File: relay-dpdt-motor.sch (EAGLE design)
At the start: 4 parts, among them K1 4052

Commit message: eagle prewired
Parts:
- added D1: 1N4004, adafruit:1N4004
- added J1, J2: 1X2-3.5MM, adafruit:1X2-3.5MM
- added JP1: (no value), adafruit:PINHD-1X3CB
- added R2: (no value), adafruit:R-US_0204/7
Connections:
- new net +12V: D1.C, J1.2, K11.1, K12.P
- new net GND: J1.1, JP1.1, Q1.E, Q2.S
- new net N$1: Q1.B, R1.2
- new net N$2: K11.2, Q1.C
- new net N$3: Q2.G, R2.2
- new net N$5: D1.A, K13.P, Q2.D
- new net N$6: J2.1, K12.S, K13.O
- new net N$7: J2.2, K12.O, K13.S
- new net N$8: JP1.2, R2.1
- new net N$9: JP1.3, R1.1
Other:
- moved on the sheet: K1, Q1, Q2, R1
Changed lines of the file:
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@@
 <setting verticaltext="up"/>
 </settings>
-<grid distance="0.1" unitdist="inch" unit="inch" style="lines" multiple="1" display="no" altdistance="0.01" altunitdist="inch" altunit="inch"/>
+<grid distance="50" unitdist="mil" unit="mil" style="lines" multiple="1" display="no" altdistance="25" altunitdist="mil" altunit="mil"/>
 <layers>
 <layer number="1" name="Top" color="4" fill="1" visible="no" active="no"/>
@@
 <part name="R1" library="adafruit" deviceset="R-US_" device="0204/7"/>
 <part name="Q2" library="adafruit" deviceset="MOSFET-N" device="GDS_TO220V"/>
+<part name="D1" library="adafruit" deviceset="1N4004" device=""/>
+<part name="J1" library="adafruit" deviceset="1X2" device="-3.5MM"/>
+<part name="+12V1" library="dp_devices" deviceset="SUPPLY_+12V" device=""/>
+<part name="R2" library="adafruit" deviceset="R-US_" device="0204/7"/>
+<part name="U$2" library="microbuilder" deviceset="GND" device=""/>
+<part name="J2" library="adafruit" deviceset="1X2" device="-3.5MM"/>
+<part name="JP1" library="adafruit" deviceset="PINHD-1X3" device="CB"/>
+<part name="U$3" library="microbuilder" deviceset="GND" device=""/>
+<part name="U$1" library="microbuilder" deviceset="GND" device=""/>
 </parts>
 <sheets>
@@
 </plain>
 <instances>
-<instance part="K1" gate="1" x="34.29" y="76.2"/>
-<instance part="K1" gate="2" x="52.07" y="76.2"/>
-<instance part="K1" gate="3" x="52.07" y="60.96"/>
-<instance part="Q1" gate="Q" x="30.48" y="57.15"/>
-<instance part="R1" gate="G$1" x="22.86" y="44.45"/>
-<instance part="Q2" gate="G$1" x="33.02" y="38.1"/>
+<instance part="K1" gate="1" x="25.4" y="74.93" smashed="yes">
+<attribute name="VALUE" x="29.21" y="70.231" size="1.778" layer="96"/>
+<attribute name="PART" x="19.05" y="77.47" size="1.778" layer="95"/>
+</instance>
+<instance part="K1" gate="2" x="50.8" y="80.01" smashed="yes" rot="R270">
+<attribute name="PART" x="50.8" y="77.47" size="1.778" layer="95" rot="R270"/>
+</instance>
+<instance part="K1" gate="3" x="50.8" y="63.5" smashed="yes" rot="R270">
+<attribute name="PART" x="50.8" y="60.96" size="1.778" layer="95" rot="R270"/>
+</instance>
+<instance part="Q1" gate="Q" x="22.86" y="63.5"/>
+<instance part="R1" gate="G$1" x="13.97" y="63.5"/>
+<instance part="Q2" gate="G$1" x="43.18" y="54.61"/>
+<instance part="D1" gate="1" x="45.72" y="71.12" smashed="yes" rot="R90">
+<attribute name="NAME" x="43.18" y="73.1774" size="1.778" layer="95" rot="R180"/>
+</instance>
+<instance part="J1" gate="G$1" x="1.27" y="80.01" rot="R180"/>
+<instance part="+12V1" gate="SUPPLY" x="25.4" y="82.55"/>
+<instance part="R2" gate="G$1" x="34.29" y="52.07"/>
+<instance part="U$2" gate="G$1" x="45.72" y="45.72"/>
+<instance part="J2" gate="G$1" x="76.2" y="71.12"/>
+<instance part="JP1" gate="A" x="6.35" y="52.07" rot="R180"/>
+<instance part="U$3" gate="G$1" x="25.4" y="46.99"/>
+<instance part="U$1" gate="G$1" x="6.35" y="73.66"/>
 </instances>
 <busses>
 </busses>
 <nets>
+<net name="N$1" class="0">
+<segment>
+<pinref part="Q1" gate="Q" pin="B"/>
+<pinref part="R1" gate="G$1" pin="2"/>
+<wire x1="19.05" y1="63.5" x2="20.32" y2="63.5" width="0.1524" layer="91"/>
+</segment>
+</net>
+<net name="+12V" class="0">
+<segment>
+<pinref part="K1" gate="2" pin="P"/>
+<pinref part="D1" gate="1" pin="C"/>
+<wire x1="45.72" y1="80.01" x2="48.26" y2="80.01" width="0.1524" layer="91"/>
+<wire x1="45.72" y1="80.01" x2="45.72" y2="73.66" width="0.1524" layer="91"/>
+<junction x="45.72" y="80.01"/>
+<pinref part="+12V1" gate="SUPPLY" pin="+12V"/>
+<pinref part="K1" gate="1" pin="1"/>
+<wire x1="25.4" y1="82.55" x2="25.4" y2="80.01" width="0.1524" layer="91"/>
+<wire x1="45.72" y1="80.01" x2="25.4" y2="80.01" width="0.1524" layer="91"/>
+<junction x="25.4" y="80.01"/>
+<pinref part="J1" gate="G$1" pin="2"/>
+<wire x1="25.4" y1="80.01" x2="6.35" y2="80.01" width="0.1524" layer="91"/>
+</segment>
+</net>
+<net name="N$2" class="0">
+<segment>
+<pinref part="K1" gate="1" pin="2"/>
+<pinref part="Q1" gate="Q" pin="C"/>
+<wire x1="25.4" y1="69.85" x2="25.4" y2="68.58" width="0.1524" layer="91"/>
+</segment>
+</net>
+<net name="GND" class="0">
+<segment>
+<pinref part="Q2" gate="G$1" pin="S"/>
+<pinref part="U$2" gate="G$1" pin="GND"/>
+<wire x1="45.72" y1="49.53" x2="45.72" y2="48.26" width="0.1524" layer="91"/>
+</segment>
+<segment>
+<pinref part="U$3" gate="G$1" pin="GND"/>
+<pinref part="JP1" gate="A" pin="1"/>
+<wire x1="25.4" y1="49.53" x2="8.89" y2="49.53" width="0.1524" layer="91"/>
+<pinref part="Q1" gate="Q" pin="E"/>
+<wire x1="25.4" y1="58.42" x2="25.4" y2="49.53" width="0.1524" layer="91"/>
+<junction x="25.4" y="49.53"/>
+</segment>
+<segment>
+<pinref part="J1" gate="G$1" pin="1"/>
+<pinref part="U$1" gate="G$1" pin="GND"/>
+<wire x1="6.35" y1="77.47" x2="6.35" y2="76.2" width="0.1524" layer="91"/>
+</segment>
+</net>
+<net name="N$3" class="0">
+<segment>
+<pinref part="Q2" gate="G$1" pin="G"/>
+<pinref part="R2" gate="G$1" pin="2"/>
+<wire x1="39.37" y1="52.07" x2="40.64" y2="52.07" width="0.1524" layer="91"/>
+</segment>
+</net>
+<net name="N$5" class="0">
+<segment>
+<pinref part="K1" gate="3" pin="P"/>
+<wire x1="48.26" y1="63.5" x2="45.72" y2="63.5" width="0.1524" layer="91"/>
+<pinref part="Q2" gate="G$1" pin="D"/>
+<wire x1="45.72" y1="63.5" x2="45.72" y2="59.69" width="0.1524" layer="91"/>
+<pinref part="D1" gate="1" pin="A"/>
+<wire x1="45.72" y1="68.58" x2="45.72" y2="63.5" width="0.1524" layer="91"/>
+<junction x="45.72" y="63.5"/>
+</segment>
+</net>
+<net name="N$6" class="0">
+<segment>
+<pinref part="K1" gate="2" pin="S"/>
+<wire x1="55.88" y1="85.09" x2="62.23" y2="85.09" width="0.1524" layer="91"/>
+<wire x1="62.23" y1="85.09" x2="68.58" y2="85.09" width="0.1524" layer="91"/>
+<wire x1="68.58" y1="85.09" x2="71.12" y2="82.55" width="0.1524" layer="91"/>
+<pinref part="J2" gate="G$1" pin="1"/>
+<wire x1="71.12" y1="82.55" x2="71.12" y2="73.66" width="0.1524" layer="91"/>
+<pinref part="K1" gate="3" pin="O"/>
+<wire x1="55.88" y1="58.42" x2="62.23" y2="58.42" width="0.1524" layer="91"/>
+<wire x1="62.23" y1="58.42" x2="62.23" y2="85.09" width="0.1524" layer="91"/>
+<junction x="62.23" y="85.09"/>
+</segment>
+</net>
+<net name="N$7" class="0">
+<segment>
+<pinref part="J2" gate="G$1" pin="2"/>
+<pinref part="K1" gate="3" pin="S"/>
+<wire x1="71.12" y1="71.12" x2="58.42" y2="71.12" width="0.1524" layer="91"/>
+<wire x1="58.42" y1="71.12" x2="55.88" y2="68.58" width="0.1524" layer="91"/>
+<pinref part="K1" gate="2" pin="O"/>
+<wire x1="55.88" y1="74.93" x2="55.88" y2="68.58" width="0.1524" layer="91"/>
+<junction x="55.88" y="68.58"/>
+</segment>
+</net>
+<net name="N$8" class="0">
+<segment>
+<pinref part="R2" gate="G$1" pin="1"/>
+<pinref part="JP1" gate="A" pin="2"/>
+<wire x1="8.89" y1="52.07" x2="29.21" y2="52.07" width="0.1524" layer="91"/>
+</segment>
+</net>
+<net name="N$9" class="0">
+<segment>
+<pinref part="R1" gate="G$1" pin="1"/>
+<pinref part="JP1" gate="A" pin="3"/>
+<wire x1="8.89" y1="63.5" x2="8.89" y2="54.61" width="0.1524" layer="91"/>
+</segment>
+</net>
 </nets>
 </sheet>

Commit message: with pnp
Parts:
- removed Q2: (no value), adafruit:MOSFET-NGDS_TO220V
- added Q3: (no value), dp_devices:TRANSISTOR_BJT_NPN-TO-92-EBC
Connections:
- removed net N$5: D1.A, K13.P, Q2.D
- new net N$4: D1.C, K12.P, Q3.E
- net +12V: now also Q3.C; no longer D1.C, K12.P
- net GND: now also D1.A, K13.P; no longer Q2.S
- net N$3: now also Q3.B; no longer Q2.G
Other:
- moved on the sheet: D1, K1
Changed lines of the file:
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@@
 <part name="Q1" library="dp_devices" deviceset="TRANSISTOR_BJT_NPN" device="-TO-92-EBC"/>
 <part name="R1" library="adafruit" deviceset="R-US_" device="0204/7"/>
-<part name="Q2" library="adafruit" deviceset="MOSFET-N" device="GDS_TO220V"/>
 <part name="D1" library="adafruit" deviceset="1N4004" device=""/>
 <part name="J1" library="adafruit" deviceset="1X2" device="-3.5MM"/>
-<part name="+12V1" library="dp_devices" deviceset="SUPPLY_+12V" device=""/>
 <part name="R2" library="adafruit" deviceset="R-US_" device="0204/7"/>
 <part name="U$2" library="microbuilder" deviceset="GND" device=""/>
@@
 <part name="U$3" library="microbuilder" deviceset="GND" device=""/>
 <part name="U$1" library="microbuilder" deviceset="GND" device=""/>
+<part name="Q3" library="dp_devices" deviceset="TRANSISTOR_BJT_NPN" device="-TO-92-EBC"/>
+<part name="+12V2" library="dp_devices" deviceset="SUPPLY_+12V" device=""/>
 </parts>
 <sheets>
@@
 <attribute name="PART" x="19.05" y="77.47" size="1.778" layer="95"/>
 </instance>
-<instance part="K1" gate="2" x="50.8" y="80.01" smashed="yes" rot="R270">
-<attribute name="PART" x="50.8" y="77.47" size="1.778" layer="95" rot="R270"/>
+<instance part="K1" gate="2" x="53.34" y="45.72" smashed="yes" rot="R270">
+<attribute name="PART" x="53.34" y="43.18" size="1.778" layer="95" rot="R270"/>
 </instance>
-<instance part="K1" gate="3" x="50.8" y="63.5" smashed="yes" rot="R270">
-<attribute name="PART" x="50.8" y="60.96" size="1.778" layer="95" rot="R270"/>
+<instance part="K1" gate="3" x="53.34" y="29.21" smashed="yes" rot="R270">
+<attribute name="PART" x="53.34" y="26.67" size="1.778" layer="95" rot="R270"/>
 </instance>
 <instance part="Q1" gate="Q" x="22.86" y="63.5"/>
 <instance part="R1" gate="G$1" x="13.97" y="63.5"/>
-<instance part="Q2" gate="G$1" x="43.18" y="54.61"/>
-<instance part="D1" gate="1" x="45.72" y="71.12" smashed="yes" rot="R90">
-<attribute name="NAME" x="43.18" y="73.1774" size="1.778" layer="95" rot="R180"/>
+<instance part="D1" gate="1" x="48.26" y="36.83" smashed="yes" rot="R90">
+<attribute name="NAME" x="45.72" y="38.8874" size="1.778" layer="95" rot="R180"/>
 </instance>
-<instance part="J1" gate="G$1" x="1.27" y="80.01" rot="R180"/>
-<instance part="+12V1" gate="SUPPLY" x="25.4" y="82.55"/>
+<instance part="J1" gate="G$1" x="-10.16" y="86.36" rot="R180"/>
 <instance part="R2" gate="G$1" x="34.29" y="52.07"/>
-<instance part="U$2" gate="G$1" x="45.72" y="45.72"/>
-<instance part="J2" gate="G$1" x="76.2" y="71.12"/>
+<instance part="U$2" gate="G$1" x="48.26" y="24.13"/>
+<instance part="J2" gate="G$1" x="78.74" y="36.83"/>
 <instance part="JP1" gate="A" x="6.35" y="52.07" rot="R180"/>
 <instance part="U$3" gate="G$1" x="25.4" y="46.99"/>
-<instance part="U$1" gate="G$1" x="6.35" y="73.66"/>
+<instance part="U$1" gate="G$1" x="-2.54" y="80.01"/>
+<instance part="Q3" gate="Q" x="45.72" y="52.07"/>
+<instance part="+12V2" gate="SUPPLY" x="-2.54" y="86.36"/>
 </instances>
 <busses>
@@
 <net name="+12V" class="0">
 <segment>
-<pinref part="K1" gate="2" pin="P"/>
-<pinref part="D1" gate="1" pin="C"/>
-<wire x1="45.72" y1="80.01" x2="48.26" y2="80.01" width="0.1524" layer="91"/>
-<wire x1="45.72" y1="80.01" x2="45.72" y2="73.66" width="0.1524" layer="91"/>
-<junction x="45.72" y="80.01"/>
-<pinref part="+12V1" gate="SUPPLY" pin="+12V"/>
+<pinref part="J1" gate="G$1" pin="2"/>
+<pinref part="+12V2" gate="SUPPLY" pin="+12V"/>
+<wire x1="-2.54" y1="86.36" x2="-5.08" y2="86.36" width="0.1524" layer="91"/>
+</segment>
+<segment>
 <pinref part="K1" gate="1" pin="1"/>
 <wire x1="25.4" y1="82.55" x2="25.4" y2="80.01" width="0.1524" layer="91"/>
-<wire x1="45.72" y1="80.01" x2="25.4" y2="80.01" width="0.1524" layer="91"/>
-<junction x="25.4" y="80.01"/>
-<pinref part="J1" gate="G$1" pin="2"/>
-<wire x1="25.4" y1="80.01" x2="6.35" y2="80.01" width="0.1524" layer="91"/>
+<label x="25.4" y="82.55" size="1.778" layer="95"/>
+</segment>
+<segment>
+<pinref part="Q3" gate="Q" pin="C"/>
+<wire x1="48.26" y1="57.15" x2="48.26" y2="60.96" width="0.1524" layer="91"/>
+<label x="48.26" y="59.69" size="1.778" layer="95"/>
 </segment>
 </net>
@@
 <net name="GND" class="0">
 <segment>
-<pinref part="Q2" gate="G$1" pin="S"/>
 <pinref part="U$2" gate="G$1" pin="GND"/>
-<wire x1="45.72" y1="49.53" x2="45.72" y2="48.26" width="0.1524" layer="91"/>
+<pinref part="K1" gate="3" pin="P"/>
+<wire x1="50.8" y1="29.21" x2="48.26" y2="29.21" width="0.1524" layer="91"/>
+<pinref part="D1" gate="1" pin="A"/>
+<wire x1="48.26" y1="34.29" x2="48.26" y2="29.21" width="0.1524" layer="91"/>
+<wire x1="48.26" y1="29.21" x2="48.26" y2="26.67" width="0.1524" layer="91"/>
+<junction x="48.26" y="29.21"/>
 </segment>
 <segment>
@@
 <pinref part="J1" gate="G$1" pin="1"/>
 <pinref part="U$1" gate="G$1" pin="GND"/>
-<wire x1="6.35" y1="77.47" x2="6.35" y2="76.2" width="0.1524" layer="91"/>
+<wire x1="-5.08" y1="83.82" x2="-2.54" y2="83.82" width="0.1524" layer="91"/>
+<wire x1="-2.54" y1="83.82" x2="-2.54" y2="82.55" width="0.1524" layer="91"/>
 </segment>
 </net>
 <net name="N$3" class="0">
 <segment>
-<pinref part="Q2" gate="G$1" pin="G"/>
 <pinref part="R2" gate="G$1" pin="2"/>
-<wire x1="39.37" y1="52.07" x2="40.64" y2="52.07" width="0.1524" layer="91"/>
-</segment>
-</net>
-<net name="N$5" class="0">
-<segment>
-<pinref part="K1" gate="3" pin="P"/>
-<wire x1="48.26" y1="63.5" x2="45.72" y2="63.5" width="0.1524" layer="91"/>
-<pinref part="Q2" gate="G$1" pin="D"/>
-<wire x1="45.72" y1="63.5" x2="45.72" y2="59.69" width="0.1524" layer="91"/>
-<pinref part="D1" gate="1" pin="A"/>
-<wire x1="45.72" y1="68.58" x2="45.72" y2="63.5" width="0.1524" layer="91"/>
-<junction x="45.72" y="63.5"/>
+<wire x1="39.37" y1="52.07" x2="43.18" y2="52.07" width="0.1524" layer="91"/>
+<pinref part="Q3" gate="Q" pin="B"/>
 </segment>
 </net>
@@
 <segment>
 <pinref part="K1" gate="2" pin="S"/>
-<wire x1="55.88" y1="85.09" x2="62.23" y2="85.09" width="0.1524" layer="91"/>
-<wire x1="62.23" y1="85.09" x2="68.58" y2="85.09" width="0.1524" layer="91"/>
-<wire x1="68.58" y1="85.09" x2="71.12" y2="82.55" width="0.1524" layer="91"/>
+<wire x1="58.42" y1="50.8" x2="64.77" y2="50.8" width="0.1524" layer="91"/>
+<wire x1="64.77" y1="50.8" x2="71.12" y2="50.8" width="0.1524" layer="91"/>
+<wire x1="71.12" y1="50.8" x2="73.66" y2="48.26" width="0.1524" layer="91"/>
 <pinref part="J2" gate="G$1" pin="1"/>
-<wire x1="71.12" y1="82.55" x2="71.12" y2="73.66" width="0.1524" layer="91"/>
+<wire x1="73.66" y1="48.26" x2="73.66" y2="39.37" width="0.1524" layer="91"/>
 <pinref part="K1" gate="3" pin="O"/>
-<wire x1="55.88" y1="58.42" x2="62.23" y2="58.42" width="0.1524" layer="91"/>
-<wire x1="62.23" y1="58.42" x2="62.23" y2="85.09" width="0.1524" layer="91"/>
-<junction x="62.23" y="85.09"/>
+<wire x1="58.42" y1="24.13" x2="64.77" y2="24.13" width="0.1524" layer="91"/>
+<wire x1="64.77" y1="24.13" x2="64.77" y2="50.8" width="0.1524" layer="91"/>
+<junction x="64.77" y="50.8"/>
 </segment>
 </net>
@@
 <pinref part="J2" gate="G$1" pin="2"/>
 <pinref part="K1" gate="3" pin="S"/>
-<wire x1="71.12" y1="71.12" x2="58.42" y2="71.12" width="0.1524" layer="91"/>
-<wire x1="58.42" y1="71.12" x2="55.88" y2="68.58" width="0.1524" layer="91"/>
+<wire x1="73.66" y1="36.83" x2="60.96" y2="36.83" width="0.1524" layer="91"/>
+<wire x1="60.96" y1="36.83" x2="58.42" y2="34.29" width="0.1524" layer="91"/>
 <pinref part="K1" gate="2" pin="O"/>
-<wire x1="55.88" y1="74.93" x2="55.88" y2="68.58" width="0.1524" layer="91"/>
-<junction x="55.88" y="68.58"/>
+<wire x1="58.42" y1="40.64" x2="58.42" y2="34.29" width="0.1524" layer="91"/>
+<junction x="58.42" y="34.29"/>
 </segment>
 </net>
@@
 </segment>
 </net>
+<net name="N$4" class="0">
+<segment>
+<pinref part="D1" gate="1" pin="C"/>
+<pinref part="K1" gate="2" pin="P"/>
+<wire x1="48.26" y1="45.72" x2="50.8" y2="45.72" width="0.1524" layer="91"/>
+<wire x1="48.26" y1="45.72" x2="48.26" y2="39.37" width="0.1524" layer="91"/>
+<pinref part="Q3" gate="Q" pin="E"/>
+<wire x1="48.26" y1="46.99" x2="48.26" y2="45.72" width="0.1524" layer="91"/>
+<junction x="48.26" y="45.72"/>
+</segment>
+</net>

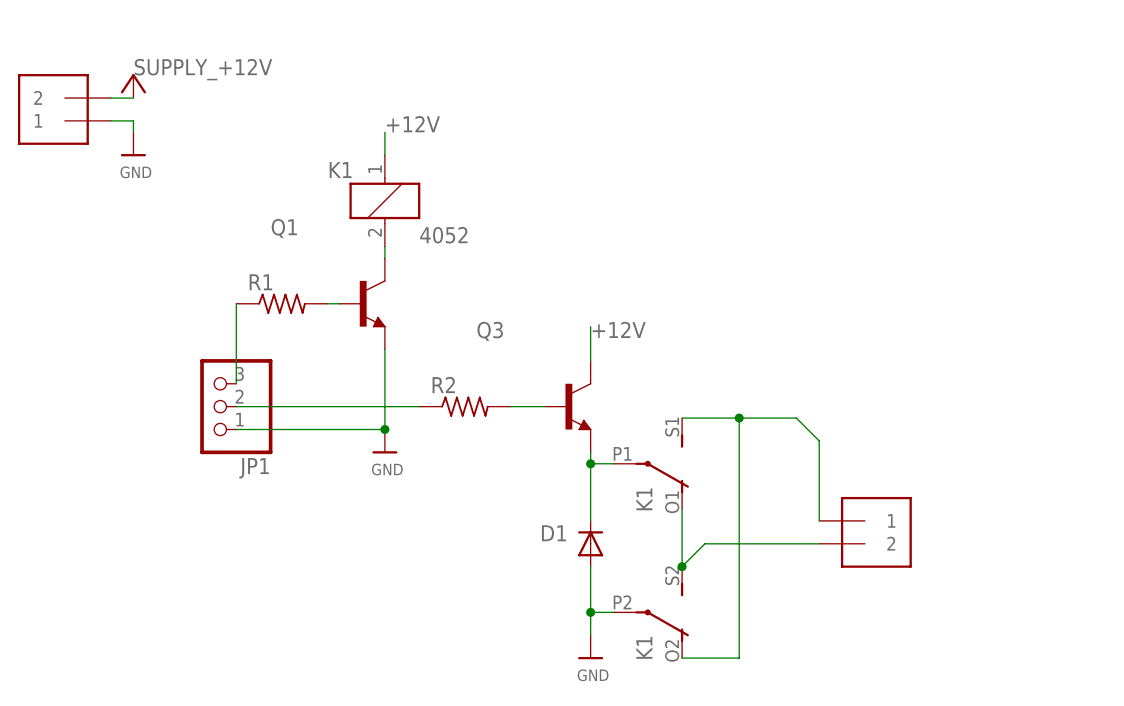
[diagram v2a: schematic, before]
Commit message: 2 relays one cup, including flyback
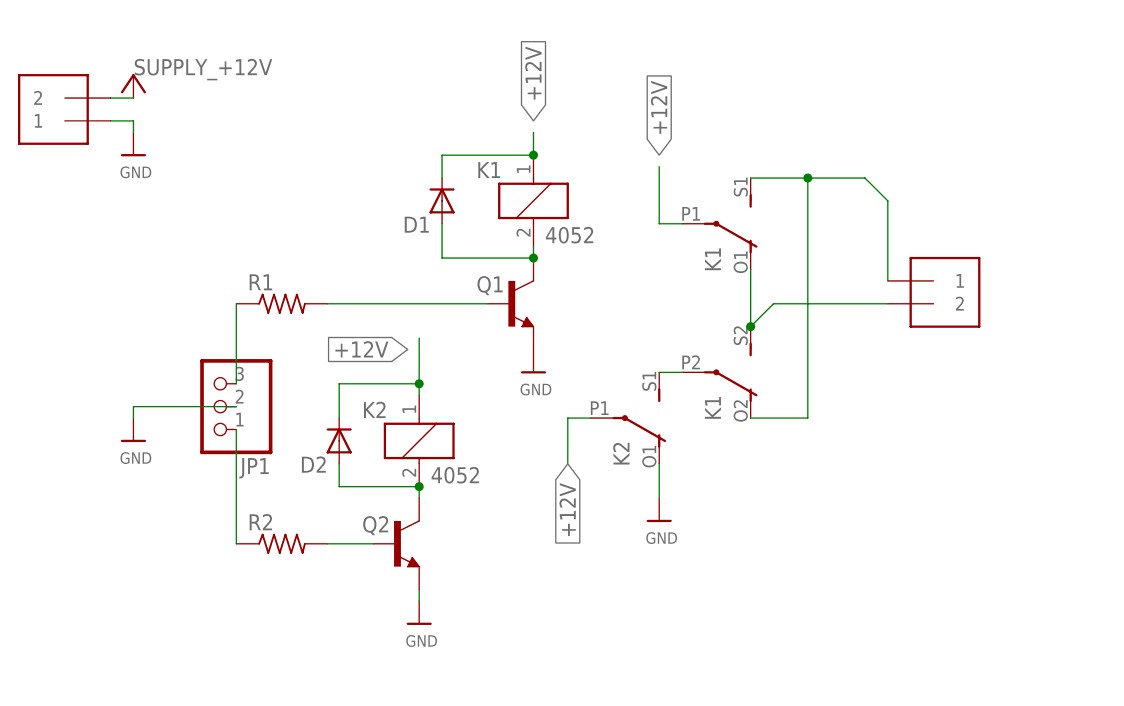
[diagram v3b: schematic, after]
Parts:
- removed Q3: (no value), dp_devices:TRANSISTOR_BJT_NPN-TO-92-EBC
- added D2: 1N4004, adafruit:1N4004
- added K2: 4052, relay:4052
- added Q2: (no value), dp_devices:TRANSISTOR_BJT_NPN-TO-92-EBC
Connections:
- removed net N$4: D1.C, K12.P, Q3.E
- new net N$10: K13.P, K22.S
- new net N$5: JP1.1, R2.1
- net +12V: now also D1.C, D2.C, K12.P, K21.1, K22.P; no longer Q3.C
- net GND: now also JP1.2, K22.O, Q2.E; no longer D1.A, JP1.1, K13.P
- net N$2: now also D1.A
- net N$3: now also Q2.B; no longer Q3.B
- net N$8: now also D2.A, K21.2, Q2.C; no longer JP1.2, R2.1
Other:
- moved on the sheet: D1, K1, Q1, R2
